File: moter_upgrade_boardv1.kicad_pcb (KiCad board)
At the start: 2 copper layers, 51 parts, among them J1 Conn_01x04_Socket, J2 Conn_01x03_Socket, J3 Conn_01x03_Socket, J4 Conn_01x02_Socket, J5 Conn_01x05_Socket, J6 USB_C_Receptacle_USB2.0_16P, J7 Conn_01x02_Socket, SW1 SW_SPDT, SW2 SW_Push, SW3 SW_Wuerth_450301014042, U1 BD33FC0FP, U2 TLP785, U3 TLP785, U4 STM32H523CCTx, U5 MCP2562-E-P, U6 CH340E, U7 BD33FC0FP

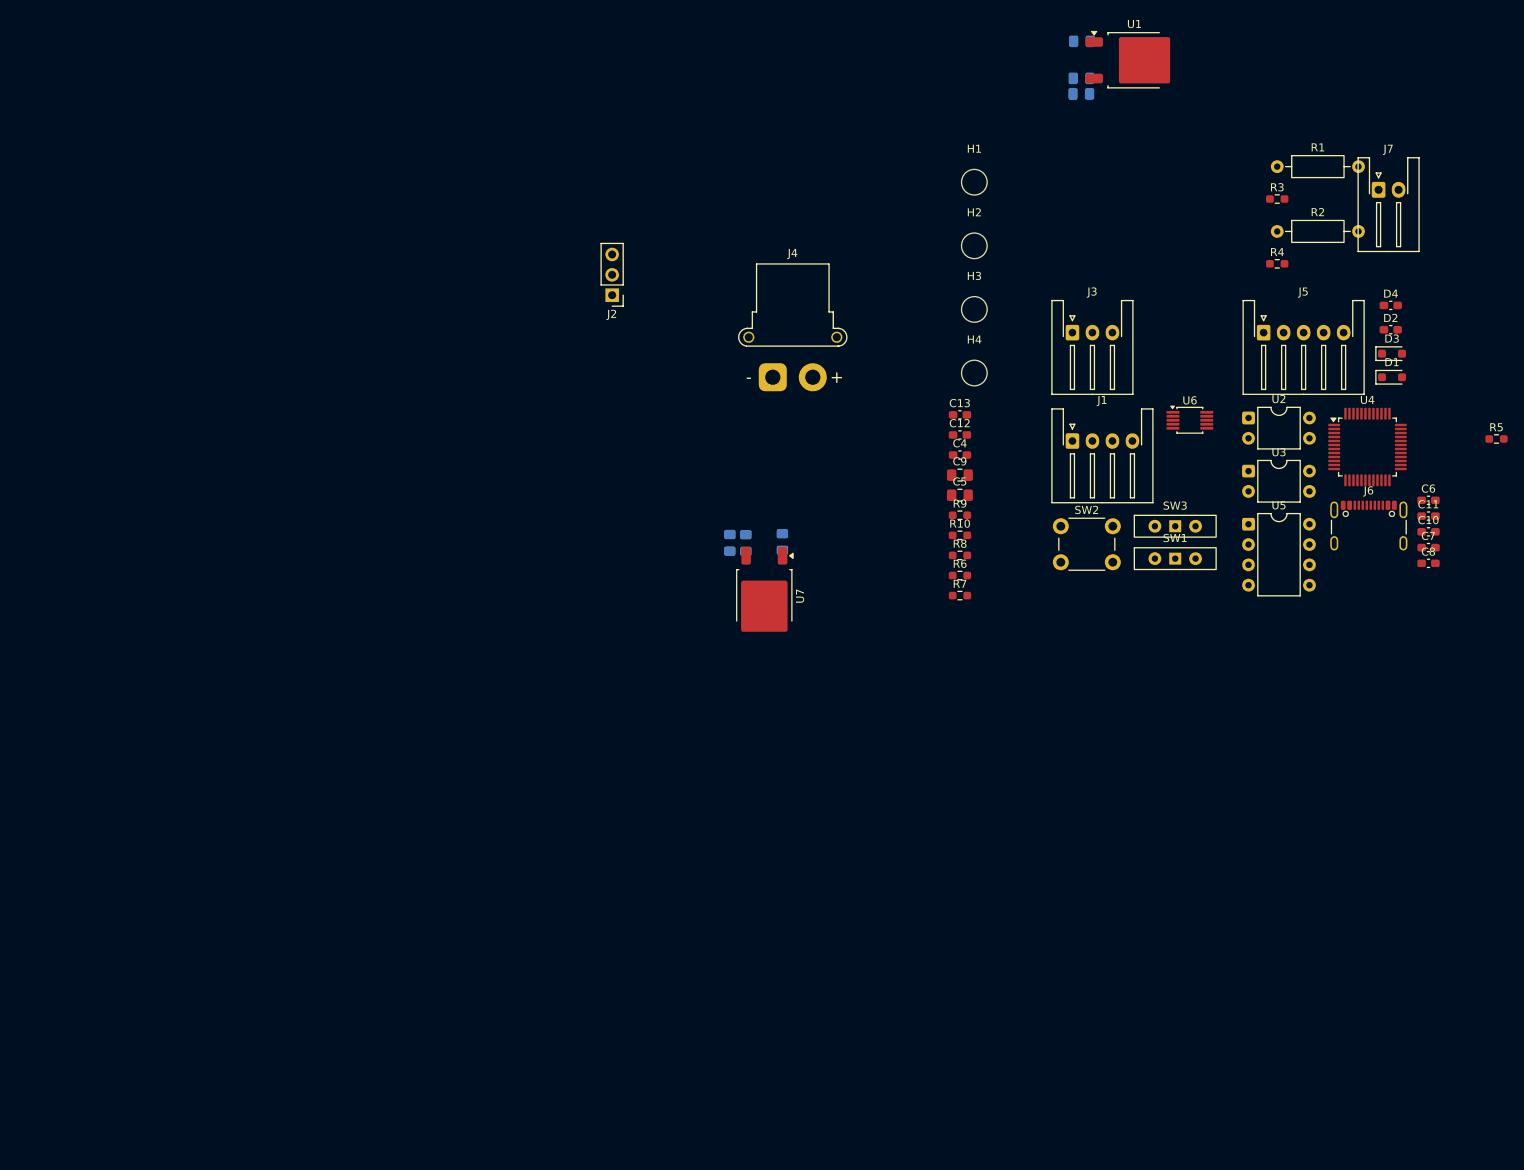
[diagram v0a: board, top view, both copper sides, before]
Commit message: フットプリントの一部変更と部品配置
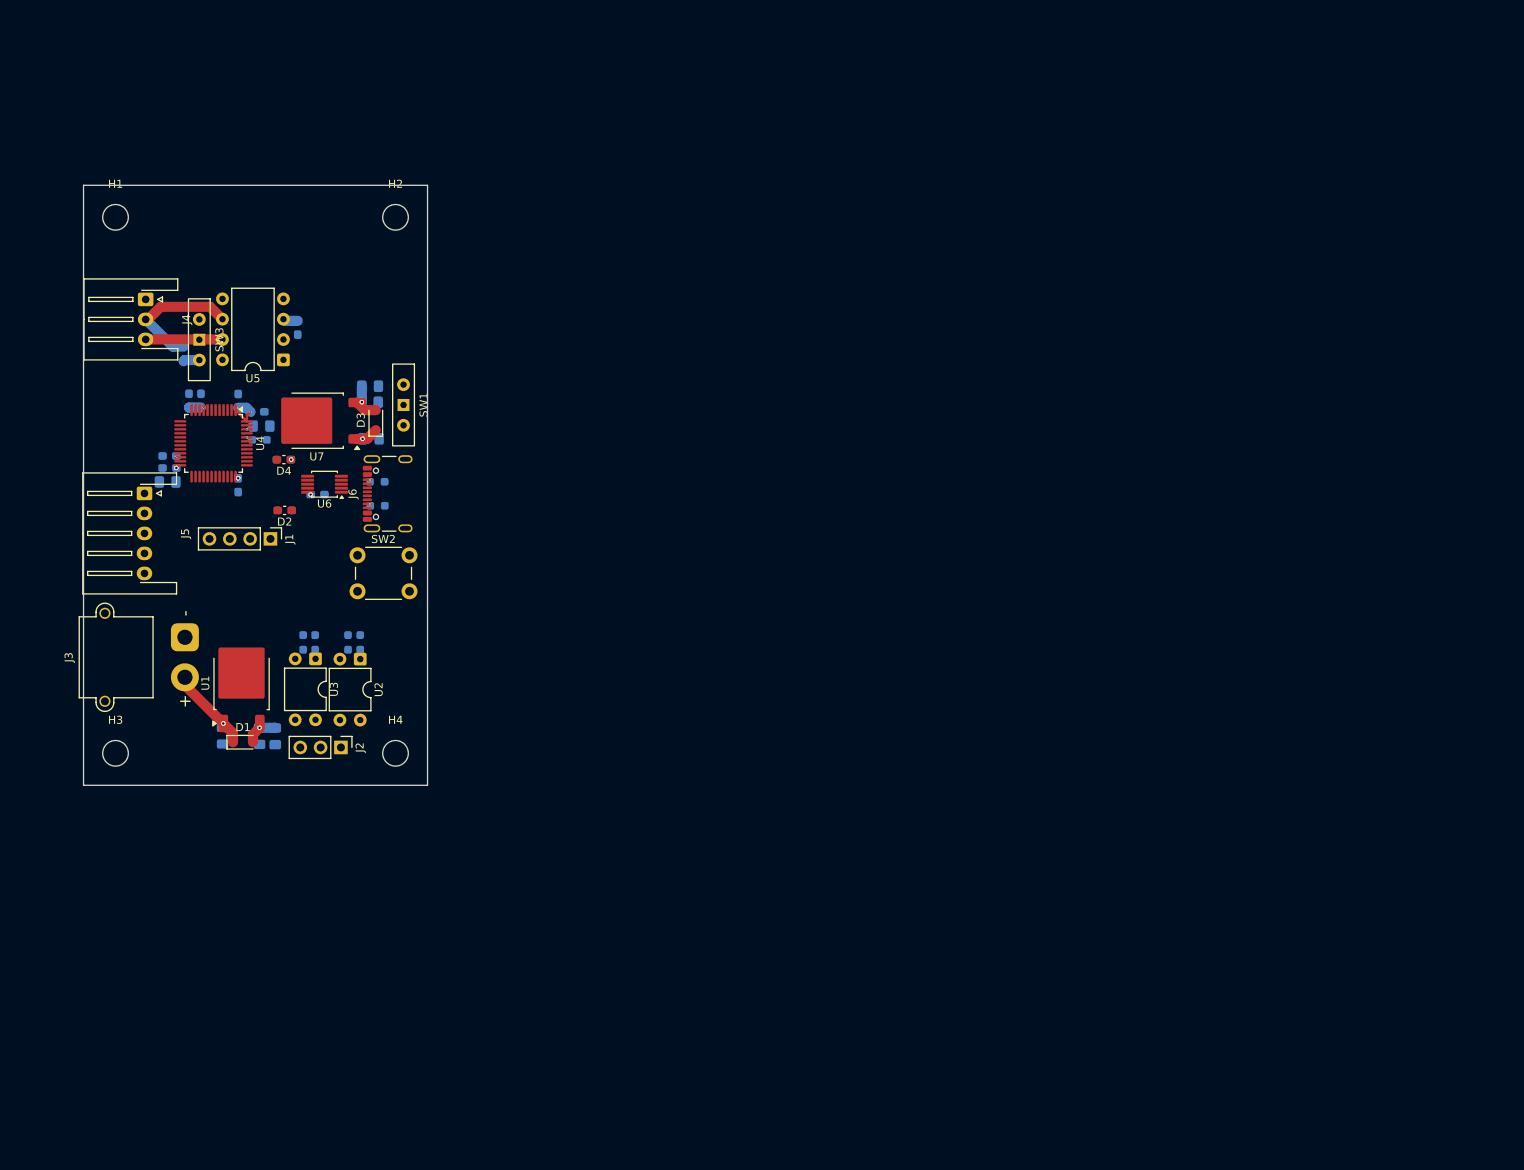
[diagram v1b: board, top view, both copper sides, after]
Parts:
- removed the J4 at (136.2, 74.0)
- removed J7: Conn_01x02_Socket, Connector_JST:JST_XH_S2B-XH-A-1_1x02_P2.50mm_Horizontal
- added C14: 1uf, Capacitor_SMD:C_0603_1608Metric_Pad1.08x0.95mm_HandSolder, B.Cu at (79.3, 88.7)
- added J3: Conn_01x02_Socket, Connector_AMASS:AMASS_XT30PW-M_1x02_P2.50mm_Horizontal, F.Cu at (62.7, 106.5)
- C10, C11, C12, C13, C4, C5, C6, C7, C8, C9, R10, R3, R4, R5, R6, R7, R8, R9: moved to B.Cu
- J1: footprint Connector_JST:JST_XH_S4B-XH-A-1_1x04_P2.50mm_Horizontal -> Connector_PinHeader_2.54mm:PinHeader_1x04_P2.54mm_Vertical
- R1, R2: footprint Resistor_THT:R_Axial_DIN0207_L6.3mm_D2.5mm_P10.16mm_Horizontal -> Resistor_SMD:R_0603_1608Metric_Pad0.98x0.95mm_HandSolder; moved to B.Cu
- moved C7 157.7 mm to (60.7, 85.3), turned to 180 degrees
- moved R5 154.6 mm to (72.0, 81.8)
- moved C11 154.1 mm to (64.7, 76.9), turned to -90 degrees
- moved D1 150.7 mm to (69.9, 119.6)
- moved C6 149.3 mm to (69.3, 76.9), turned to 90 degrees
- moved C8 149.1 mm to (69.3, 87.5), turned to -90 degrees
- moved C10 147.1 mm to (71.7, 78.3)
- moved U4 144.2 mm to (66.3, 82.3), turned to -90 degrees
- moved J5 141.3 mm to (57.6, 88.5), turned to -90 degrees
- moved D2 140.1 mm to (75.1, 90.6), turned to 180 degrees
- moved D4 139.7 mm to (75.0, 84.3), turned to 180 degrees
- moved C1 138.1 mm to (67.4, 118.8), turned to -90 degrees
- moved U1 136.1 mm to (69.8, 112.2), turned to 90 degrees
- moved R2 132.2 mm to (77.5, 107.1), turned to -90 degrees
- moved C3 131.6 mm to (72.0, 118.8), turned to -90 degrees
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- renumbered C14 to C15, C15 to C16, C16 to C17, J3 to J4
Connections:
- U4 pad 26: en-x -> en-b
- U4 pad 28: en-b -> en-x
- U6 pad 10: unconnected-(U6-V3-Pad10) -> Net-(U6-V3)
- U6 pad 7: unconnected-(U6-VCC-Pad7) -> +5V
- U6 pad 8: unconnected-(U6-TXD-Pad8) -> uart1-tx
- U6 pad 9: unconnected-(U6-RXD-Pad9) -> uart1-rx
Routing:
- net CAN_L: track 0.00 -> 17.0 mm
- net +3.3V: track 0.00 -> 13.2 mm, vias 0 -> 6
- net +24V: track 0.00 -> 10.6 mm, vias 0 -> 1
- net CAN_H: track 0.00 -> 9.61 mm
- net +5V: track 0.00 -> 4.66 mm, vias 0 -> 1
- net +3V3: track 0.00 -> 4.11 mm, vias 0 -> 1
- net CANR: track 0.00 -> 2.04 mm
- net Net-(C5-Pad2): track 0.00 -> 0.96 mm, vias 0 -> 1
- net Net-(C4-Pad2): track 0.00 -> 0.93 mm, vias 0 -> 1
- net BOOT0: track 0.00 -> 0.80 mm, vias 0 -> 1
- net Net-(U6-V3): track 0.00 -> 0.51 mm, vias 0 -> 1
- net Net-(J6-CC1): track 0.00 -> 0.37 mm, vias 0 -> 1
- net Net-(J6-CC2): track 0.00 -> 0.35 mm, vias 0 -> 1
- net Net-(D4-K): track 0.00 -> 0.05 mm, vias 0 -> 1
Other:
- board outline added: 43 x 75 mm

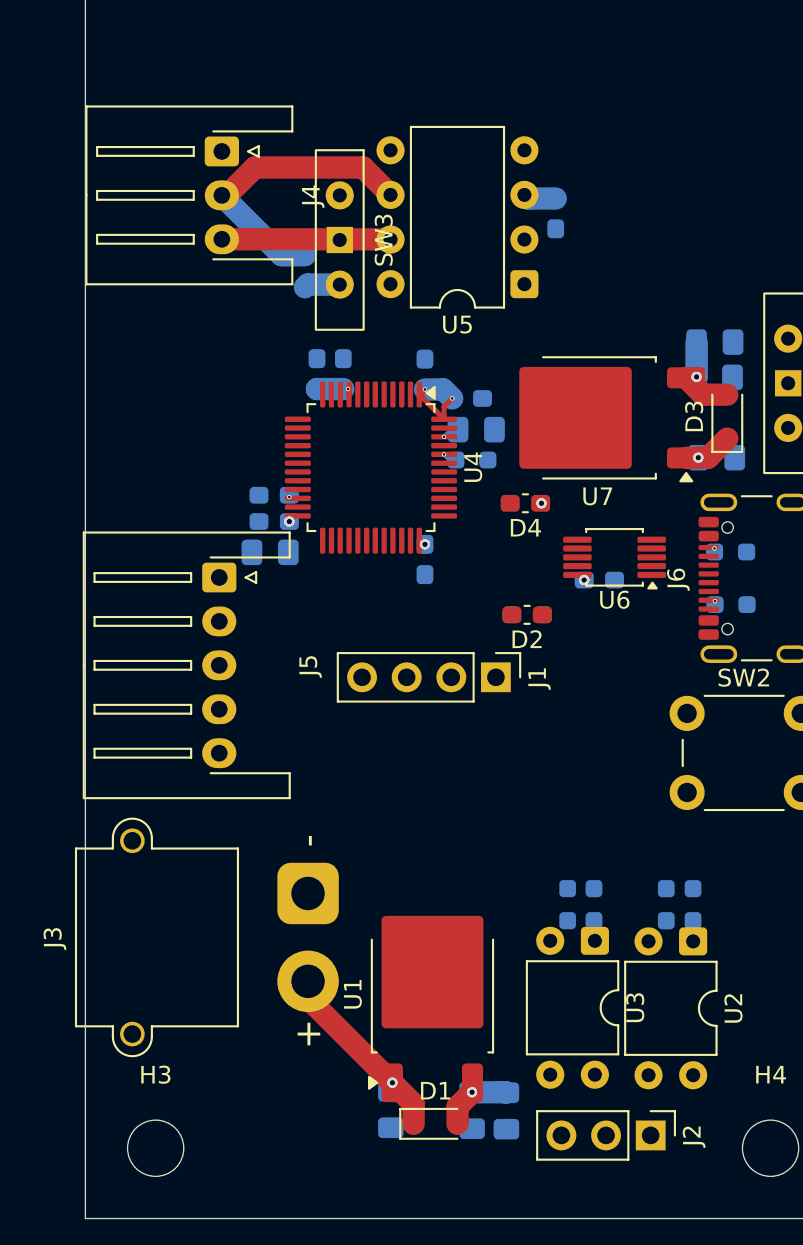
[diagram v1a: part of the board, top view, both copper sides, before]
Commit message: md13s用ブランチ作成
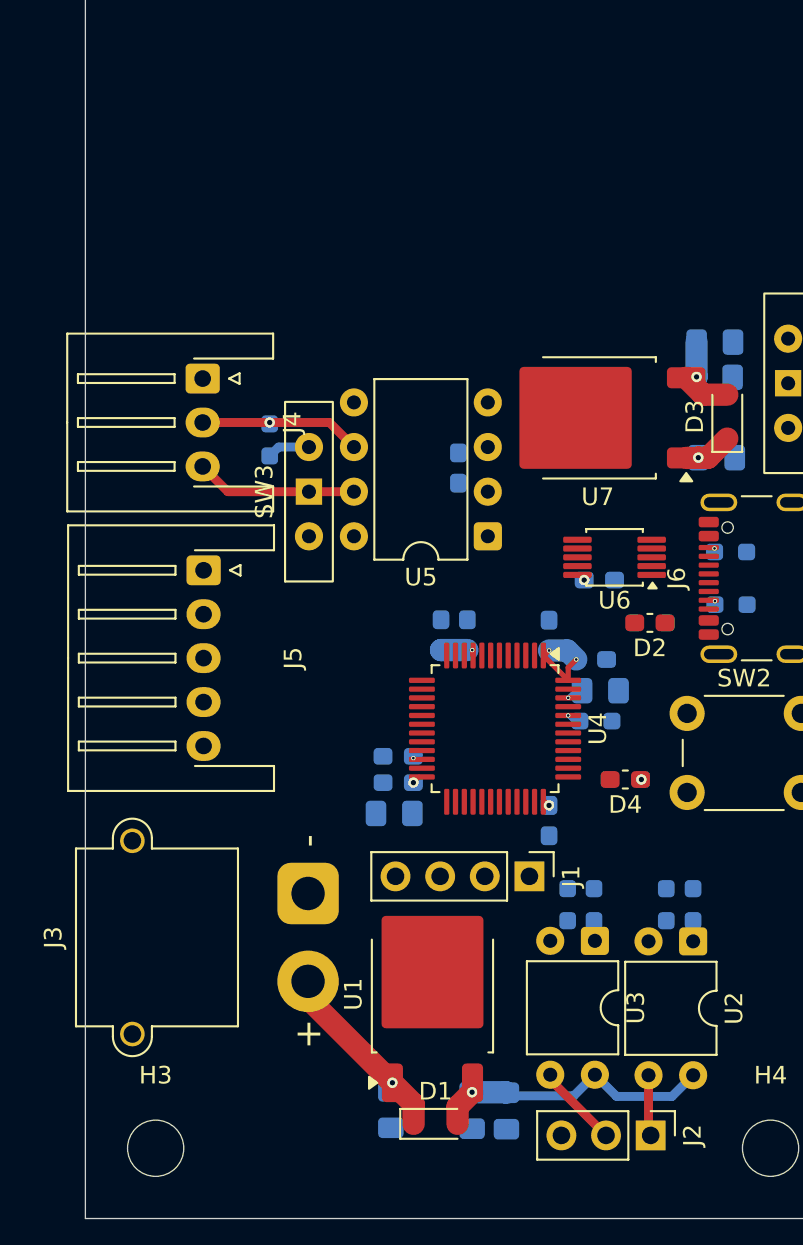
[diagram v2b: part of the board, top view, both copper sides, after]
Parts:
- moved D4 16.7 mm to (80.7, 100.0)
- moved R8 16.7 mm to (80.7, 100.0)
- moved C10 16.5 mm to (78.8, 93.2)
- moved U4 16.5 mm to (73.3, 97.1)
- moved C9 16.5 mm to (67.6, 101.9)
- moved C11 16.5 mm to (71.7, 91.8)
- moved C4 16.5 mm to (67.8, 98.7)
- moved C5 16.5 mm to (79.3, 95.0)
- moved C6 16.5 mm to (76.4, 91.8)
- moved C7 16.5 mm to (67.8, 100.2)
- moved C8 16.5 mm to (76.4, 102.3)
- moved R5 16.5 mm to (79.1, 96.7)
- moved C12 16.5 mm to (70.2, 91.8)
- moved C13 15.5 mm to (71.2, 82.3)
- moved U5 14.5 mm to (72.9, 86.2)
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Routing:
- net +3V3: track 4.11 -> 16.3 mm
- net CAN_L: track 17.0 -> 9.26 mm, vias 0 -> 1
- net Net-(J2-Pin_2): track 0.00 -> 4.77 mm
- net Net-(J2-Pin_1): track 0.00 -> 3.47 mm
- net +5V: track 4.66 -> 2.79 mm

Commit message: 配線、配置変更など　いったん完成
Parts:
- moved C11 15.7 mm to (71.8, 76.1)
- moved C12 15.7 mm to (70.3, 76.1)
- moved R6 14.5 mm to (60.5, 66.2)
- moved R10 14.5 mm to (87.9, 75.6)
- moved R9 14.5 mm to (87.9, 72.6)
- moved J2 14.4 mm to (79.5, 106.1)
- moved R2 14.4 mm to (77.5, 92.7)
- moved C4 14.2 mm to (66.8, 84.5)
- moved C5 14.2 mm to (79.9, 80.8)
- moved C10 14.2 mm to (78.8, 79.0)
- moved C14 14.2 mm to (79.3, 74.5)
- moved C15 14.2 mm to (85.9, 67.5)
- moved D2 14.2 mm to (82.1, 76.9)
- moved D4 14.2 mm to (80.7, 85.8)
- moved J5 14.2 mm to (56.7, 73.9)
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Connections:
- J6 pad S1: unconnected-(J6-SHIELD-PadS1)_1 -> GND
- U4 pad 13: wm to moter -> unconnected-(U4-PA3-Pad13)
- U4 pad 14: dir to moter -> unconnected-(U4-PA4-Pad14)
- U4 pad 29: unconnected-(U4-PA8-Pad29) -> wm to moter
- U4 pad 30: unconnected-(U4-PA9-Pad30) -> dir to moter
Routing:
- net +3.3V: track 13.2 -> 93.7 mm, vias 6 -> 7
- net +5V: track 2.79 -> 48.1 mm, vias 1 -> 4
- net GND: track 0.00 -> 41.8 mm, vias 0 -> 41
- net nrst: track 0.00 -> 34.1 mm, vias 0 -> 2
- net BOOT0: track 0.80 -> 29.8 mm
- net CAN2rx: track 0.00 -> 27.3 mm, vias 0 -> 1
- net en-b: track 0.00 -> 22.8 mm
- net en-a: track 0.00 -> 20.2 mm
- net en-x: track 0.00 -> 20.1 mm
- net CAN2tx: track 0.00 -> 16.3 mm, vias 0 -> 1
- net Net-(D2-A): track 0.00 -> 15.4 mm
- net uart1-tx: track 0.00 -> 14.9 mm, vias 0 -> 2
- net dir to moter: track 0.00 -> 13.7 mm, vias 0 -> 1
- net uart1-rx: track 0.00 -> 12.4 mm, vias 0 -> 2
- net wm to moter: track 0.00 -> 8.39 mm, vias 0 -> 1
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- added copper zone on B.Cu, net GND
- added copper zone on F.Cu, net GND
- added copper zone on B.Cu, net GND1
- added copper zone on F.Cu, net GND1
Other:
- board size 43 x 75 mm -> 43 x 61.2 mm
- board text added: "G-Low-High"
- board text added: "G-Pwm-Dir"
- board text added: "ON-OFF"
- board text added: "b-V-a-x-G"

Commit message: CAN端子の追加
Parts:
- added J7: Conn_01x03_Socket, Connector_JST:JST_XH_B3B-XH-A_1x03_P2.50mm_Vertical, F.Cu at (64.9, 59.9)
- moved J4 20.4 mm to (76.2, 57.1), turned to 180 degrees
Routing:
- net CAN_H: track 9.21 -> 26.9 mm
- net CAN_L: track 9.19 -> 23.9 mm, vias 1 -> 2
- net GND: vias 41 -> 37

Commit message: usbCをもとに戻した　最終？？版
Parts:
- added G***: LOGO, LOGO, B.Cu at (69.8, 57.7)
- R8: value 120 -> 1k
- moved R9 0.51 mm to (88.4, 72.7)
- moved R10 0.48 mm to (88.4, 75.5)
- moved J6 0.21 mm to (89.3, 74.2)
- moved C13 0.16 mm to (71.2, 67.9)
- moved C3 0.16 mm to (70.0, 105.2)
- moved C5 0.16 mm to (79.9, 80.6)
- moved C6 0.16 mm to (76.4, 77.4)
- moved C7 0.16 mm to (67.8, 85.8)
- moved C8 0.16 mm to (76.4, 88.0)
- moved C9 0.16 mm to (67.6, 87.6)
- moved D3 0.16 mm to (86.5, 65.0)
- moved H3 0.16 mm to (54.0, 106.6)
- moved H4 0.16 mm to (89.0, 106.6)
- moved J1 0.16 mm to (75.3, 91.2)
- moved R1 0.16 mm to (83.1, 92.8)
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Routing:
- net GND1: track 0.00 -> 19.2 mm
- net GND: track 41.8 -> 54.2 mm, vias 37 -> 36
- net d+: track 5.03 -> 6.22 mm
- net +5V: track 48.1 -> 47.3 mm
- net Net-(D2-K): track 0.00 -> 0.05 mm, vias 0 -> 1
- net CAN_L: vias 2 -> 1
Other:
- board size 43 x 61.2 mm -> 43 x 61 mm

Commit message: 回路図の書き換え　部品配置配線のリセット
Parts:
- removed C1, C15, C16, C2: 4.7μF, Capacitor_SMD:C_0805_2012Metric_Pad1.18x1.45mm_HandSolder
- removed C10, C6, C7, C8: 0.1uF, Capacitor_SMD:C_0603_1608Metric_Pad1.08x0.95mm_HandSolder
- removed C11, C13: 0.1uf, Capacitor_SMD:C_0603_1608Metric_Pad1.08x0.95mm_HandSolder
- removed C12, C14: 1uf, Capacitor_SMD:C_0603_1608Metric_Pad1.08x0.95mm_HandSolder
- removed C17, C3: 22μF, Capacitor_SMD:C_0805_2012Metric_Pad1.18x1.45mm_HandSolder
- removed C4: 2.2μF, Capacitor_SMD:C_0603_1608Metric_Pad1.08x0.95mm_HandSolder
- removed C5: 2.2μF, Capacitor_SMD:C_0805_2012Metric_Pad1.18x1.45mm_HandSolder
- removed C9: 4.7uf, Capacitor_SMD:C_0805_2012Metric_Pad1.18x1.45mm_HandSolder
- removed D1, D3: D_Shockley, Diode_SMD:D_SOD-323_HandSoldering
- removed D2: LED_GREEN, Capacitor_SMD:C_0603_1608Metric_Pad1.08x0.95mm_HandSolder
- removed D4: LED_RED, Capacitor_SMD:C_0603_1608Metric_Pad1.08x0.95mm_HandSolder
- removed H1, H2, H3, H4: MountingHole, MountingHole:MountingHole_3.2mm_M3
- removed J1: Conn_01x04_Socket, Connector_PinHeader_2.54mm:PinHeader_1x04_P2.54mm_Vertical
- removed J2: Conn_01x03_Socket, Connector_PinHeader_2.54mm:PinHeader_1x03_P2.54mm_Vertical
- removed J3: Conn_01x02_Socket, Connector_AMASS:AMASS_XT30PW-M_1x02_P2.50mm_Horizontal
- removed J4: Conn_01x03_Socket, Connector_JST:JST_XH_S3B-XH-A-1_1x03_P2.50mm_Horizontal
- removed J5: Conn_01x05_Socket, Connector_JST:JST_XH_S5B-XH-A-1_1x05_P2.50mm_Horizontal
- removed J6: USB_C_Receptacle_USB2.0_16P, Connector_USB:USB_C_Receptacle_GCT_USB4105-xx-A_16P_TopMnt_Horizontal
- removed J7: Conn_01x03_Socket, Connector_JST:JST_XH_B3B-XH-A_1x03_P2.50mm_Vertical
- removed R1, R2: 68, Resistor_SMD:R_0603_1608Metric_Pad0.98x0.95mm_HandSolder
- removed R10, R9: 5.1k, Resistor_SMD:R_0603_1608Metric_Pad0.98x0.95mm_HandSolder
- removed R3, R4, R7, R8: 1k, Resistor_SMD:R_0603_1608Metric_Pad0.98x0.95mm_HandSolder
- removed R5: 10K, Resistor_SMD:R_0603_1608Metric_Pad0.98x0.95mm_HandSolder
- removed R6: 120, Resistor_SMD:R_0603_1608Metric_Pad0.98x0.95mm_HandSolder
- removed SW1: SW_SPDT, Button_Switch_THT:SW_Slide-03_Wuerth-WS-SLTV_10x2.5x6.4_P2.54mm
- removed SW2: SW_Push, Button_Switch_THT:SW_PUSH_6mm
- removed SW3: SW_Wuerth_450301014042, Button_Switch_THT:SW_Slide-03_Wuerth-WS-SLTV_10x2.5x6.4_P2.54mm
- removed U1, U7: BD33FC0FP, Package_TO_SOT_SMD:TO-252-2
- removed U2, U3: TLP785, Package_DIP:DIP-4_W7.62mm
- removed U4: STM32H523CCTx, Package_QFP:LQFP-48_7x7mm_P0.5mm
- removed U5: MCP2562-E-P, Package_DIP:DIP-8_W7.62mm
- removed U6: CH340E, Package_SO:MSOP-10_3x3mm_P0.5mm
- moved G*** 104.2 mm to (171.0, 32.8)
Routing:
- net +3.3V: track 93.7 -> 0.00 mm, vias 7 -> 0
- net GND: track 54.2 -> 0.00 mm, vias 36 -> 0
- net +5V: track 47.3 -> 0.00 mm, vias 4 -> 0
- net nrst: track 34.1 -> 0.00 mm, vias 2 -> 0
- net BOOT0: track 29.8 -> 0.00 mm, vias 1 -> 0
- net CAN2rx: track 27.3 -> 0.00 mm, vias 1 -> 0
- net CAN_H: track 26.9 -> 0.00 mm
- net CAN_L: track 23.9 -> 0.00 mm, vias 1 -> 0
- net en-b: track 22.8 -> 0.00 mm
- net en-a: track 20.2 -> 0.00 mm
- net en-x: track 20.1 -> 0.00 mm
- net GND1: track 19.2 -> 0.00 mm
- net +3V3: track 19.1 -> 0.00 mm, vias 1 -> 0
- net CAN2tx: track 16.3 -> 0.00 mm, vias 1 -> 0
- net Net-(D2-A): track 15.4 -> 0.00 mm
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- removed copper zone on B.Cu, net GND
- removed copper zone on F.Cu, net GND
- removed copper zone on B.Cu, net GND1
- removed copper zone on F.Cu, net GND1
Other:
- board outline removed
- board text removed: "G-Low-High"
- board text removed: "G-Pwm-Dir"
- board text removed: "ON-OFF"
- board text removed: "b-V-a-x-G"
